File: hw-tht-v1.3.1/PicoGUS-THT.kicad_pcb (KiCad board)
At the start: 2 copper layers, 103.7 x 99.8 mm, 89 parts, among them J1 IRQDMA_JP, J10 GY-PCM5102, J11 USB-A, J3 Bus_ISA_8bit, J5 SJ1-3535NG, J6 UART_TX, J7 USB power jumper, J8 SJ1-3535NG-GR, J9 Waveblaster, U1 Pico, U10 74AHCT126, U11 NE5532, U12 USBLC6-2SC6, U2 74AHC244, U3 SN74CB3T3257, U4 SN74CB3T3257, U5 74AHC14, U6 74AHC00, U7 74AHC00, U8 APS6404L-3SQR-SN, U9 PCM5100A

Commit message: THT rev B: back silkscreen links github.com/polpo/picogus
Co-Authored-By: Claude Opus 5.5 <noreply@anthropic.com>
Claude-Session: https://claude.ai/code/session_011utN3x8yYUNDvkpGCEq5yD
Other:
- board text added: "PicoGUS v1.3.1 © 2023-2026 Ian Scott (polpo), Vidar Waagbø (waagbo) Licensed under CERN-OHL-P v2 https://github.com/polpo/picogus Thanks to polpo and all the PicoGUS contributors. This revision is dedicated to my wonderful family, Mila and Alisa."
- board text removed: "PicoGUS v1.3.1 © 2023-2026 Ian Scott (polpo), Vidar Waagbø (waagbo) Licensed under CERN-OHL-P v2 https://github.com/waagbo/picogus Thanks to polpo and all the PicoGUS contributors. This revision is dedicated to my wonderful family, Mila and Alisa."
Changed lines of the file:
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@@
 		)
 	)
-	(gr_text "PicoGUS v1.3.1\n© 2023-2026 Ian Scott (polpo), Vidar Waagbø (waagbo)\n\nLicensed under CERN-OHL-P v2\nhttps://github.com/waagbo/picogus\n\nThanks to polpo and all the PicoGUS contributors.\nThis revision is dedicated to my wonderful family, Mila and Alisa."
+	(gr_text "PicoGUS v1.3.1\n© 2023-2026 Ian Scott (polpo), Vidar Waagbø (waagbo)\n\nLicensed under CERN-OHL-P v2\nhttps://github.com/polpo/picogus\n\nThanks to polpo and all the PicoGUS contributors.\nThis revision is dedicated to my wonderful family, Mila and Alisa."
 		(at 193.4 108.9 0)
 		(layer "B.SilkS")

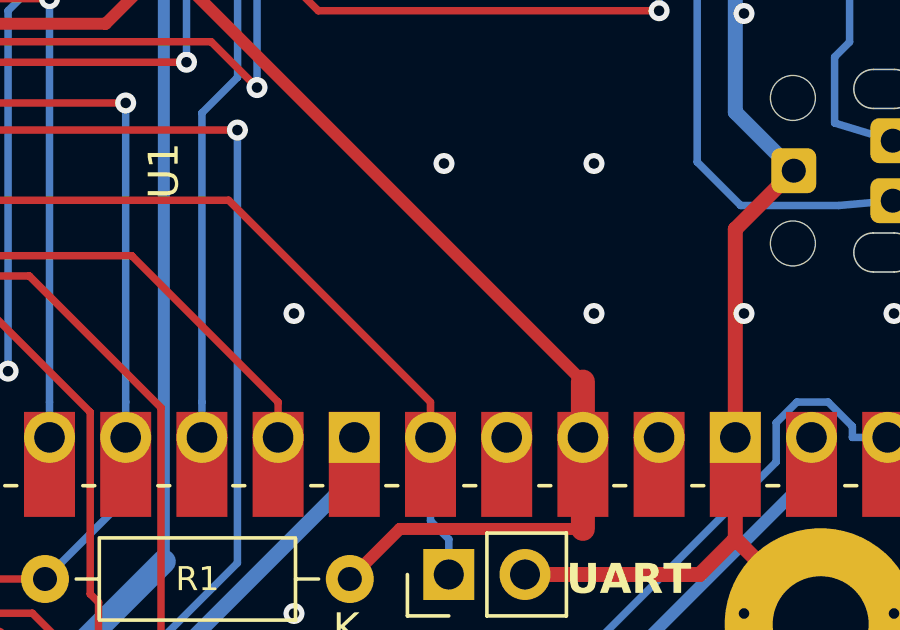
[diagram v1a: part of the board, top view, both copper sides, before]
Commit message: THT rev B: princess back artwork; keep via holes out of the back text
- Back silkscreen: hw-common/art/mila-alisa.svg (two crowned princesses,
  sparkles and a castle over the PicoGUS logo) replaces the game heroes,
  72.5 x 37 mm, logo 3 mm above the Pico pin holes, 6 mm toward the
  bracket so no pad lands in the faces. Cut 0.3 mm around pads/holes/vias.
- Back text block split into one text per line; lines nudged (<= 0.9 mm)
  so no via hole cuts a letter (the 'b' in Waagbo was cut). Two track-less
  GND stitching vias under the dedication moved <= 0.4 mm.
- DRC with schematic parity: 0 errors, 0 unconnected; warnings and silk
  DRC counts unchanged.

Co-Authored-By: Claude Opus 5.5 <noreply@anthropic.com>
Claude-Session: https://claude.ai/code/session_011utN3x8yYUNDvkpGCEq5yD
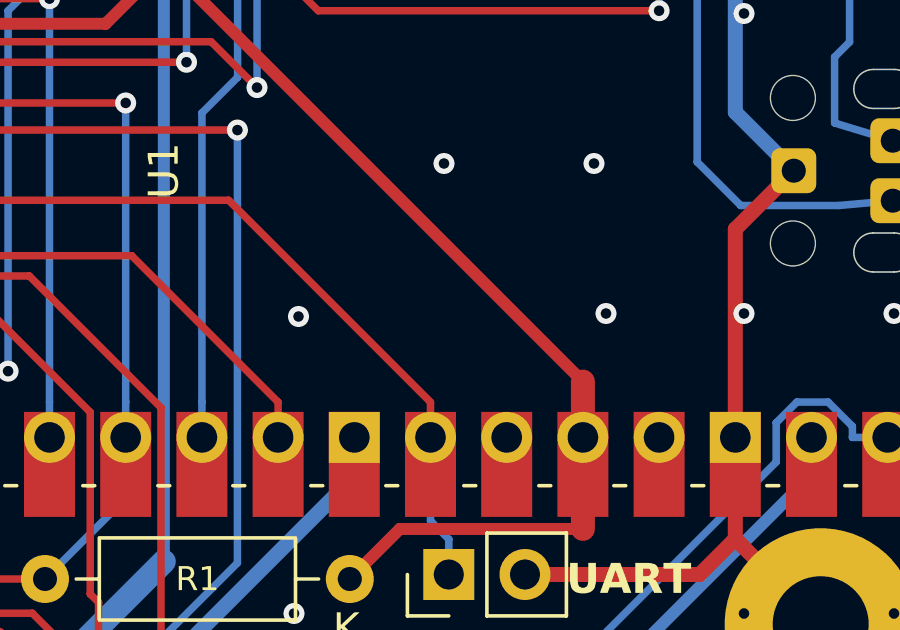
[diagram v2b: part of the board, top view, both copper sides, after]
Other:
- board text added: "Licensed under CERN-OHL-P v2"
- board text added: "PicoGUS v1.3.1"
- board text added: "Thanks to polpo and all the PicoGUS contributors."
- board text added: "This revision is dedicated to my wonderful family, Mila and Alisa."
- board text added: "https://github.com/polpo/picogus"
- board text added: "© 2023-2026 Ian Scott (polpo), Vidar Waagbø (waagbo)"
- board text removed: "PicoGUS v1.3.1 © 2023-2026 Ian Scott (polpo), Vidar Waagbø (waagbo) Licensed under CERN-OHL-P v2 https://github.com/polpo/picogus Thanks to polpo and all the PicoGUS contributors. This revision is dedicated to my wonderful family, Mila and Alisa."
